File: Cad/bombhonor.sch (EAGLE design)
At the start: 74 parts, among them CN2 TR1-01, U1 STM32L011F4P6

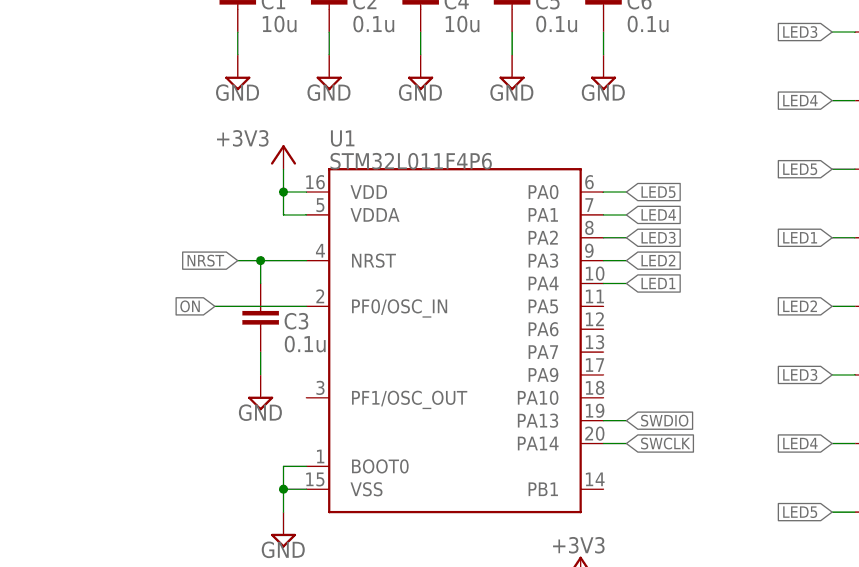
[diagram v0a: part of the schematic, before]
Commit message: Modificata scheda per avere i pin a posto con l'STM32L011. Creata fantasia su vecchia scheda. Aggiunto codice nuovo micro
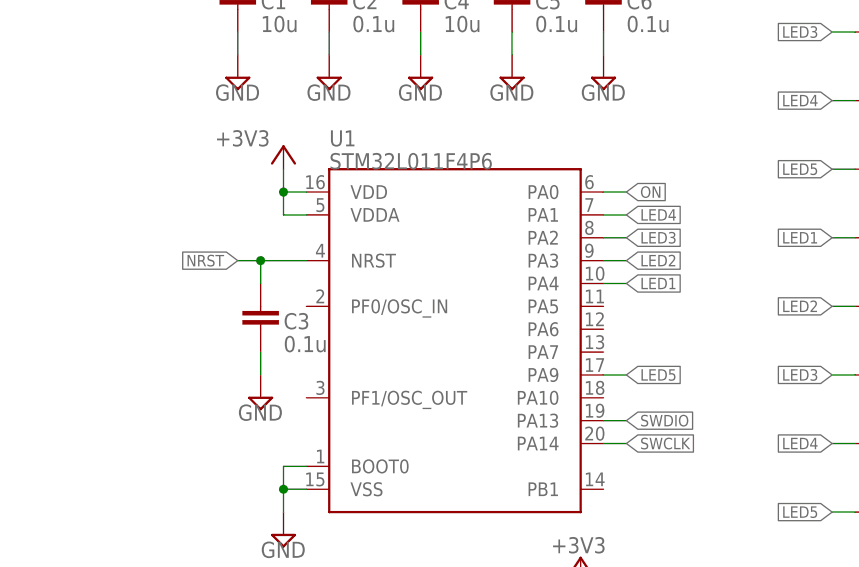
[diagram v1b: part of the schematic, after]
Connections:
- net LED5: now also U1.PA9; no longer U1.PA0
- net ON: now also U1.PA0; no longer U1.PF0/OSC_IN
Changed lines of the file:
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@@
 </segment>
 <segment>
-<wire x1="147.32" y1="134.62" x2="144.78" y2="134.62" width="0.1524" layer="91"/>
-<label x="147.32" y="134.62" size="1.27" layer="95" xref="yes"/>
-<pinref part="U1" gate="G$1" pin="PA0"/>
+<pinref part="U1" gate="G$1" pin="PA9"/>
+<wire x1="147.32" y1="114.3" x2="144.78" y2="114.3" width="0.1524" layer="91"/>
+<label x="147.32" y="114.3" size="1.27" layer="95" xref="yes"/>
 </segment>
 </net>
@@
 </segment>
 <segment>
-<wire x1="101.6" y1="121.92" x2="111.76" y2="121.92" width="0.1524" layer="91"/>
-<label x="101.6" y="121.92" size="1.27" layer="95" rot="R180" xref="yes"/>
-<pinref part="U1" gate="G$1" pin="PF0/OSC_IN"/>
-</segment>
-</net>
+<pinref part="U1" gate="G$1" pin="PA0"/>
+<wire x1="147.32" y1="134.62" x2="144.78" y2="134.62" width="0.1524" layer="91"/>
+<label x="147.32" y="134.62" size="1.27" layer="95" xref="yes"/>
+</segment>
+</net>

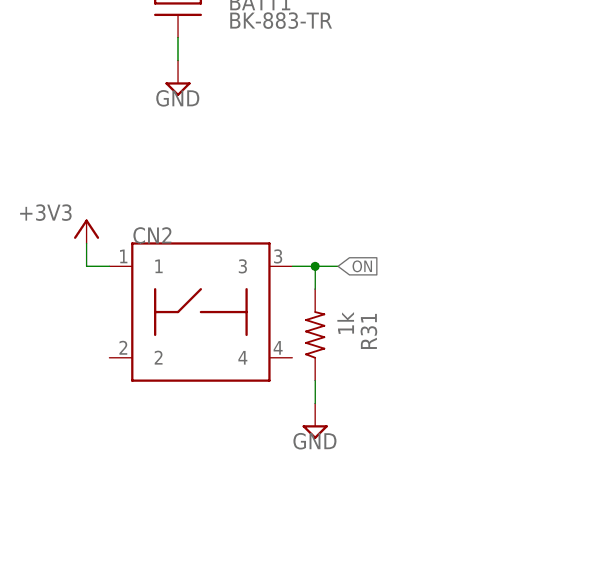
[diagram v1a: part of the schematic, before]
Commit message: Iniziata a mettere aposto la scheda. cambiato pulsante. il reset non ci sta
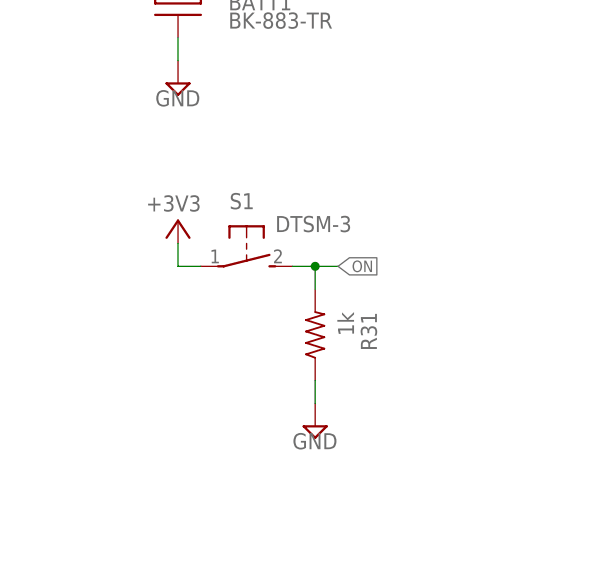
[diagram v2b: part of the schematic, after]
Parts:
- removed CN2: TR1-01, cesso:TR1-01
- added S1: DTSM-3, switch-tact:DTSM-3
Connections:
- net +3V3: now also S1.1; no longer CN2.1
- net ON: now also S1.2; no longer CN2.3
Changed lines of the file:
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@@
 </part>
 <part name="GND43" library="AlmaSUP" deviceset="GND" device=""/>
-<part name="CN2" library="cesso" deviceset="TR1-01" device="">
-<attribute name="PARTNO" value="TR1-01"/>
-</part>
 <part name="+3V9" library="AlmaSUP" deviceset="+3V3" device=""/>
 <part name="R31" library="AlmaPASS" deviceset="R" device="0603" value="1k">
@@
 <part name="GND40" library="AlmaSUP" deviceset="GND" device=""/>
 <part name="+3V10" library="AlmaSUP" deviceset="+3V3" device=""/>
+<part name="S1" library="switch-tact" deviceset="DTSM-3" device=""/>
 </parts>
 <sheets>
@@
 <attribute name="VALUE" x="43.18" y="144.78" size="1.778" layer="96"/>
 </instance>
-<instance part="CN2" gate="G$1" x="48.26" y="121.92" smashed="yes">
-<attribute name="NAME" x="40.64" y="129.54" size="1.778" layer="95"/>
-<attribute name="PARTNO" x="48.26" y="121.92" size="1.27" layer="96" display="off"/>
-</instance>
-<instance part="+3V9" gate="G$1" x="35.56" y="132.08" smashed="yes">
-<attribute name="VALUE" x="27.94" y="132.08" size="1.778" layer="96"/>
+<instance part="+3V9" gate="G$1" x="45.72" y="132.08" smashed="yes">
+<attribute name="VALUE" x="42.164" y="133.096" size="1.778" layer="96"/>
 </instance>
 <instance part="R31" gate="G$1" x="60.96" y="119.38" smashed="yes" rot="R270">
@@
 <instance part="+3V10" gate="G$1" x="142.24" y="93.98" smashed="yes">
 <attribute name="VALUE" x="138.938" y="94.488" size="1.778" layer="96"/>
+</instance>
+<instance part="S1" gate="G$1" x="53.34" y="127" smashed="yes" rot="R270">
+<attribute name="NAME" x="51.435" y="133.35" size="1.778" layer="95"/>
+<attribute name="VALUE" x="56.515" y="130.81" size="1.778" layer="96"/>
 </instance>
 </instances>
@@
 <segment>
 <pinref part="+3V9" gate="G$1" pin="+3V3"/>
-<pinref part="CN2" gate="G$1" pin="1"/>
-<wire x1="35.56" y1="129.54" x2="35.56" y2="127" width="0.1524" layer="91"/>
-<wire x1="35.56" y1="127" x2="38.1" y2="127" width="0.1524" layer="91"/>
+<wire x1="45.72" y1="129.54" x2="45.72" y2="127" width="0.1524" layer="91"/>
+<pinref part="S1" gate="G$1" pin="1"/>
+<wire x1="45.72" y1="127" x2="48.26" y2="127" width="0.1524" layer="91"/>
 </segment>
 <segment>
@@
 <segment>
 <pinref part="R31" gate="G$1" pin="2"/>
-<pinref part="CN2" gate="G$1" pin="3"/>
 <wire x1="60.96" y1="124.46" x2="60.96" y2="127" width="0.1524" layer="91"/>
-<wire x1="60.96" y1="127" x2="58.42" y2="127" width="0.1524" layer="91"/>
 <wire x1="63.5" y1="127" x2="60.96" y2="127" width="0.1524" layer="91"/>
 <junction x="60.96" y="127"/>
 <label x="63.5" y="127" size="1.27" layer="95" xref="yes"/>
-</segment>
-<segment>
+<pinref part="S1" gate="G$1" pin="2"/>
+<wire x1="58.42" y1="127" x2="60.96" y2="127" width="0.1524" layer="91"/>
+</segment>
+<segment>

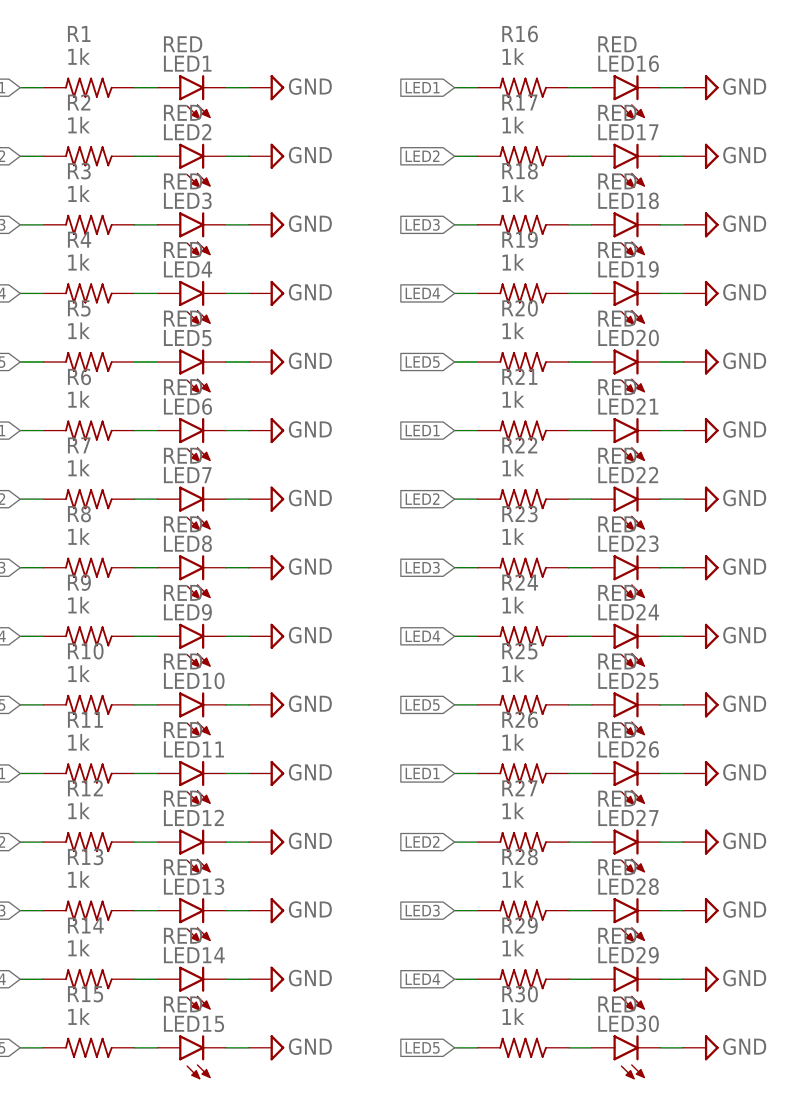
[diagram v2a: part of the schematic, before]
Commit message: Messa a posto la bom, creato excel e stime di costo
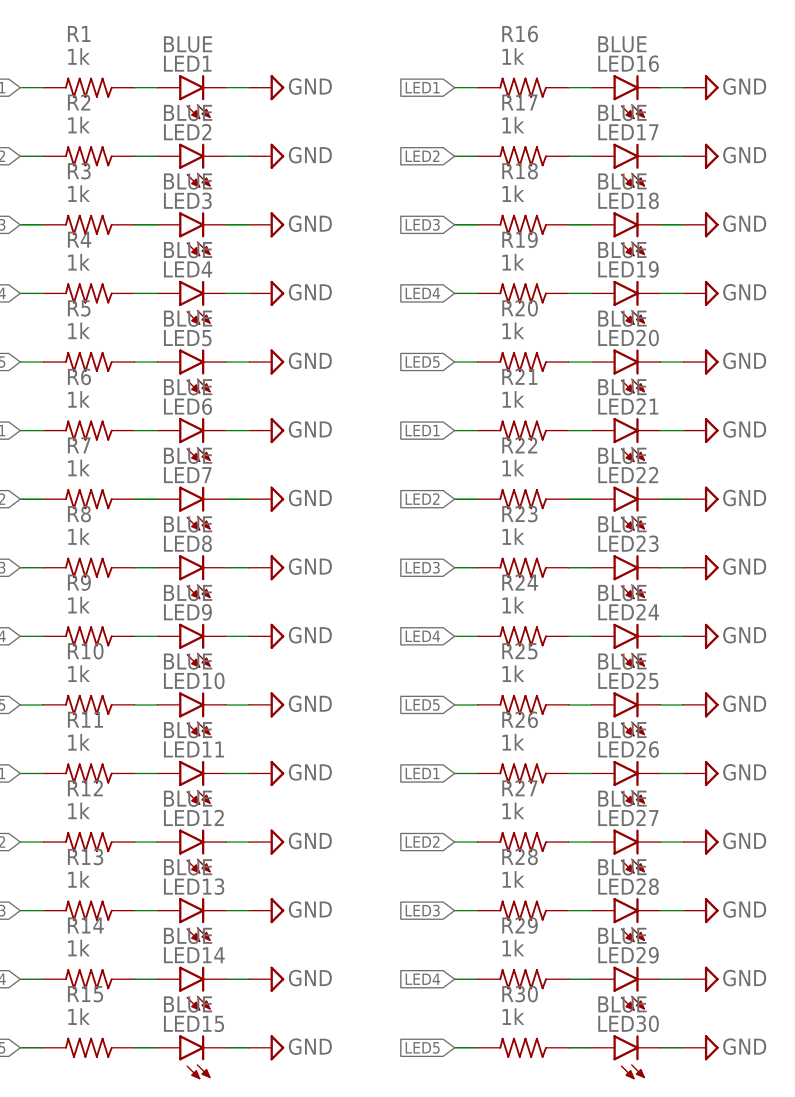
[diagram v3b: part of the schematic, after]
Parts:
- LED1, LED10, LED11, LED12, LED13, LED14, LED15, LED16, LED17, LED18, LED19, LED2, LED20, LED21, LED22, LED23, LED24, LED25, LED26, LED27, LED28, LED29, LED3, LED30, LED4, LED5, LED6, LED7, LED8, LED9: value RED -> BLUE
- S1: PARTNO (none) -> DTSM-3
- TP1, TP2, TP3, TP4: PARTNO (none) -> DNP

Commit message: cambiati part number led
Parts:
- LED1, LED10, LED11, LED12, LED13, LED14, LED15, LED16, LED17, LED18, LED19, LED2, LED20, LED21, LED22, LED23, LED24, LED25, LED26, LED27, LED28, LED29, LED3, LED30, LED4, LED5, LED6, LED7, LED8, LED9: PARTNO LTST-C230KRKT -> LTST-C230TBKT
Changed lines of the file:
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@@
 <parts>
 <part name="LED1" library="AlmaOPTO" deviceset="LED_SMD" device="1206" value="BLUE">
-<attribute name="PARTNO" value="LTST-C230KRKT"/>
+<attribute name="PARTNO" value="LTST-C230TBKT"/>
 </part>
 <part name="LED2" library="AlmaOPTO" deviceset="LED_SMD" device="1206" value="BLUE">
-<attribute name="PARTNO" value="LTST-C230KRKT"/>
+<attribute name="PARTNO" value="LTST-C230TBKT"/>
 </part>
 <part name="LED3" library="AlmaOPTO" deviceset="LED_SMD" device="1206" value="BLUE">
-<attribute name="PARTNO" value="LTST-C230KRKT"/>
+<attribute name="PARTNO" value="LTST-C230TBKT"/>
 </part>
 <part name="LED4" library="AlmaOPTO" deviceset="LED_SMD" device="1206" value="BLUE">
-<attribute name="PARTNO" value="LTST-C230KRKT"/>
+<attribute name="PARTNO" value="LTST-C230TBKT"/>
 </part>
 <part name="LED5" library="AlmaOPTO" deviceset="LED_SMD" device="1206" value="BLUE">
-<attribute name="PARTNO" value="LTST-C230KRKT"/>
+<attribute name="PARTNO" value="LTST-C230TBKT"/>
 </part>
 <part name="LED6" library="AlmaOPTO" deviceset="LED_SMD" device="1206" value="BLUE">
-<attribute name="PARTNO" value="LTST-C230KRKT"/>
+<attribute name="PARTNO" value="LTST-C230TBKT"/>
 </part>
 <part name="LED7" library="AlmaOPTO" deviceset="LED_SMD" device="1206" value="BLUE">
-<attribute name="PARTNO" value="LTST-C230KRKT"/>
+<attribute name="PARTNO" value="LTST-C230TBKT"/>
 </part>
 <part name="LED8" library="AlmaOPTO" deviceset="LED_SMD" device="1206" value="BLUE">
-<attribute name="PARTNO" value="LTST-C230KRKT"/>
+<attribute name="PARTNO" value="LTST-C230TBKT"/>
 </part>
 <part name="LED9" library="AlmaOPTO" deviceset="LED_SMD" device="1206" value="BLUE">
-<attribute name="PARTNO" value="LTST-C230KRKT"/>
+<attribute name="PARTNO" value="LTST-C230TBKT"/>
 </part>
 <part name="LED10" library="AlmaOPTO" deviceset="LED_SMD" device="1206" value="BLUE">
-<attribute name="PARTNO" value="LTST-C230KRKT"/>
+<attribute name="PARTNO" value="LTST-C230TBKT"/>
 </part>
 <part name="LED11" library="AlmaOPTO" deviceset="LED_SMD" device="1206" value="BLUE">
-<attribute name="PARTNO" value="LTST-C230KRKT"/>
+<attribute name="PARTNO" value="LTST-C230TBKT"/>
 </part>
 <part name="LED12" library="AlmaOPTO" deviceset="LED_SMD" device="1206" value="BLUE">
-<attribute name="PARTNO" value="LTST-C230KRKT"/>
+<attribute name="PARTNO" value="LTST-C230TBKT"/>
 </part>
 <part name="LED13" library="AlmaOPTO" deviceset="LED_SMD" device="1206" value="BLUE">
-<attribute name="PARTNO" value="LTST-C230KRKT"/>
+<attribute name="PARTNO" value="LTST-C230TBKT"/>
 </part>
 <part name="LED14" library="AlmaOPTO" deviceset="LED_SMD" device="1206" value="BLUE">
-<attribute name="PARTNO" value="LTST-C230KRKT"/>
+<attribute name="PARTNO" value="LTST-C230TBKT"/>
 </part>
 <part name="LED15" library="AlmaOPTO" deviceset="LED_SMD" device="1206" value="BLUE">
-<attribute name="PARTNO" value="LTST-C230KRKT"/>
+<attribute name="PARTNO" value="LTST-C230TBKT"/>
 </part>
 <part name="LED16" library="AlmaOPTO" deviceset="LED_SMD" device="1206" value="BLUE">
-<attribute name="PARTNO" value="LTST-C230KRKT"/>
+<attribute name="PARTNO" value="LTST-C230TBKT"/>
 </part>
 <part name="LED17" library="AlmaOPTO" deviceset="LED_SMD" device="1206" value="BLUE">
-<attribute name="PARTNO" value="LTST-C230KRKT"/>
+<attribute name="PARTNO" value="LTST-C230TBKT"/>
 </part>
 <part name="LED18" library="AlmaOPTO" deviceset="LED_SMD" device="1206" value="BLUE">
-<attribute name="PARTNO" value="LTST-C230KRKT"/>
+<attribute name="PARTNO" value="LTST-C230TBKT"/>
 </part>
 <part name="LED19" library="AlmaOPTO" deviceset="LED_SMD" device="1206" value="BLUE">
-<attribute name="PARTNO" value="LTST-C230KRKT"/>
+<attribute name="PARTNO" value="LTST-C230TBKT"/>
 </part>
 <part name="LED20" library="AlmaOPTO" deviceset="LED_SMD" device="1206" value="BLUE">
-<attribute name="PARTNO" value="LTST-C230KRKT"/>
+<attribute name="PARTNO" value="LTST-C230TBKT"/>
 </part>
 <part name="LED21" library="AlmaOPTO" deviceset="LED_SMD" device="1206" value="BLUE">
-<attribute name="PARTNO" value="LTST-C230KRKT"/>
+<attribute name="PARTNO" value="LTST-C230TBKT"/>
 </part>
 <part name="LED22" library="AlmaOPTO" deviceset="LED_SMD" device="1206" value="BLUE">
-<attribute name="PARTNO" value="LTST-C230KRKT"/>
+<attribute name="PARTNO" value="LTST-C230TBKT"/>
 </part>
 <part name="LED23" library="AlmaOPTO" deviceset="LED_SMD" device="1206" value="BLUE">
-<attribute name="PARTNO" value="LTST-C230KRKT"/>
+<attribute name="PARTNO" value="LTST-C230TBKT"/>
 </part>
 <part name="LED24" library="AlmaOPTO" deviceset="LED_SMD" device="1206" value="BLUE">
-<attribute name="PARTNO" value="LTST-C230KRKT"/>
+<attribute name="PARTNO" value="LTST-C230TBKT"/>
 </part>
 <part name="LED25" library="AlmaOPTO" deviceset="LED_SMD" device="1206" value="BLUE">
-<attribute name="PARTNO" value="LTST-C230KRKT"/>
+<attribute name="PARTNO" value="LTST-C230TBKT"/>
 </part>
 <part name="LED26" library="AlmaOPTO" deviceset="LED_SMD" device="1206" value="BLUE">
-<attribute name="PARTNO" value="LTST-C230KRKT"/>
+<attribute name="PARTNO" value="LTST-C230TBKT"/>
 </part>
 <part name="LED27" library="AlmaOPTO" deviceset="LED_SMD" device="1206" value="BLUE">
-<attribute name="PARTNO" value="LTST-C230KRKT"/>
+<attribute name="PARTNO" value="LTST-C230TBKT"/>
 </part>
 <part name="LED28" library="AlmaOPTO" deviceset="LED_SMD" device="1206" value="BLUE">
-<attribute name="PARTNO" value="LTST-C230KRKT"/>
+<attribute name="PARTNO" value="LTST-C230TBKT"/>
 </part>
 <part name="LED29" library="AlmaOPTO" deviceset="LED_SMD" device="1206" value="BLUE">
-<attribute name="PARTNO" value="LTST-C230KRKT"/>
+<attribute name="PARTNO" value="LTST-C230TBKT"/>
 </part>
 <part name="LED30" library="AlmaOPTO" deviceset="LED_SMD" device="1206" value="BLUE">
-<attribute name="PARTNO" value="LTST-C230KRKT"/>
+<attribute name="PARTNO" value="LTST-C230TBKT"/>
 </part>
 <part name="U1" library="AlmaIC" deviceset="STM32F030F4" device="" value="STM32L011F4P6">
